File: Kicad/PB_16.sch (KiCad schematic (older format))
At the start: 33 parts, among them J17 Power In Left, J18 Power In Right, J19 USB, J23 VIN Voltage, J24 Expansion Header, J25 RTC Conn, J26 OLED Select, J27 GPIO Header, J28 Aux Pwr, J29 VIN Select, SW2 OLED Select, SW4 Enter BTN, SW5 Down BTN, U2 LM7805, U6 24L256

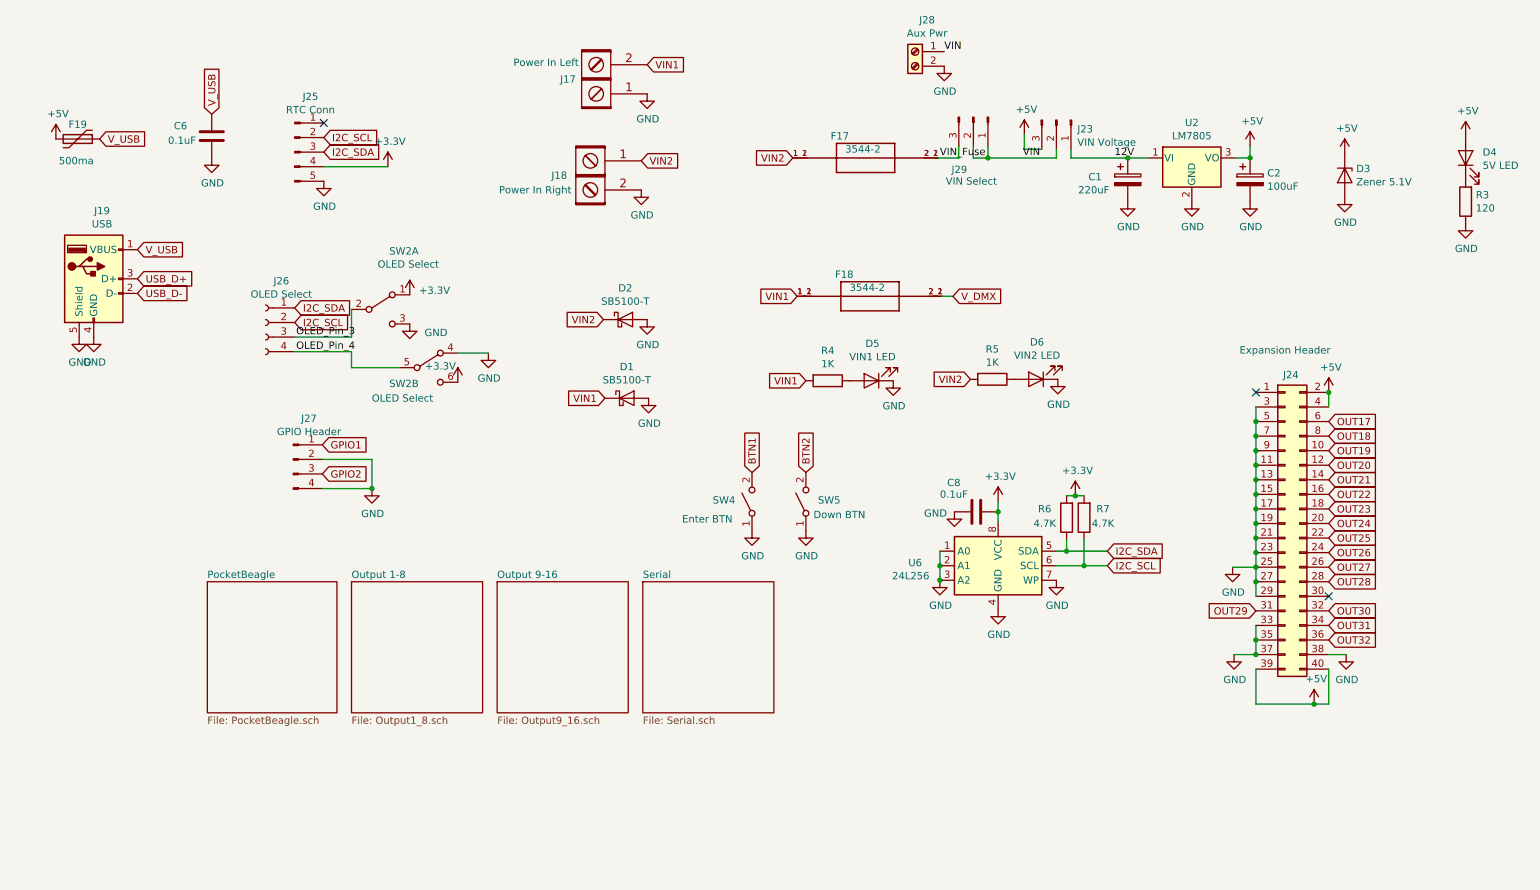
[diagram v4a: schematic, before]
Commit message: cleaning up schematic
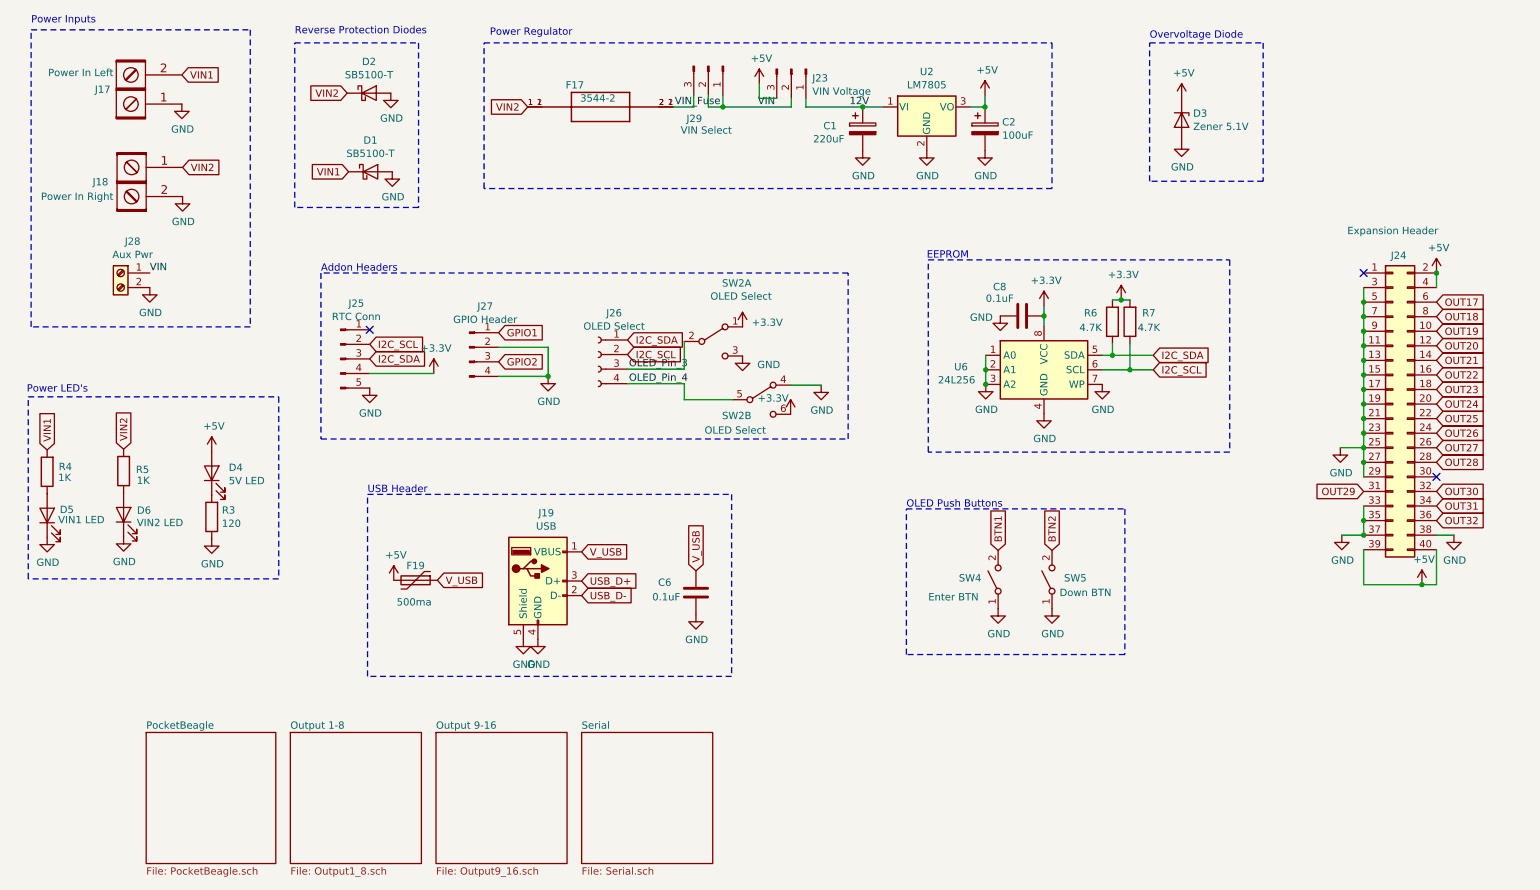
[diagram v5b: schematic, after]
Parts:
- removed F18: 3544-2, Keystone_Fuse:FUSE_3544-2, symbol PB_16-rescue:3544-2-Keystone_Fuse
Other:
- note added: "Addon Headers"
- note added: "EEPROM"
- note added: "OLED Push Buttons"
- note added: "Overvoltage Diode"
- note added: "Power Inputs"
- note added: "Power LED's"
- note added: "Power Regulator"
- note added: "Reverse Protection Diodes"
- note added: "USB Header"
- moved on the sheet: C1, C2, C6, C8, D1, D2, D3, D4, D5, D6, F17, F19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

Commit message: added BBB16 Flex
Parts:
- J19: symbol Connector:USB_A -> PB_16-rescue:USB_A-Connector
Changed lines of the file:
@@
 $EndComp
 $Comp
-L Connector:USB_A J19
+L PB_16-rescue:USB_A-Connector J19
 U 1 1 5D4E8733
 P 4270 4495
